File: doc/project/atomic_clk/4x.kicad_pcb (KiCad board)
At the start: 2 copper layers, 97.5 x 62.5 mm, 88 parts, among them J1 Goldpin, J2 Bat, SW1 POWER, SW2 SET, SW3 CLEAR, U1 BQ-M322RD, U2 STM32F030F4Px, U3 TC1185-3.3VCT8, Y1 18.432MHz

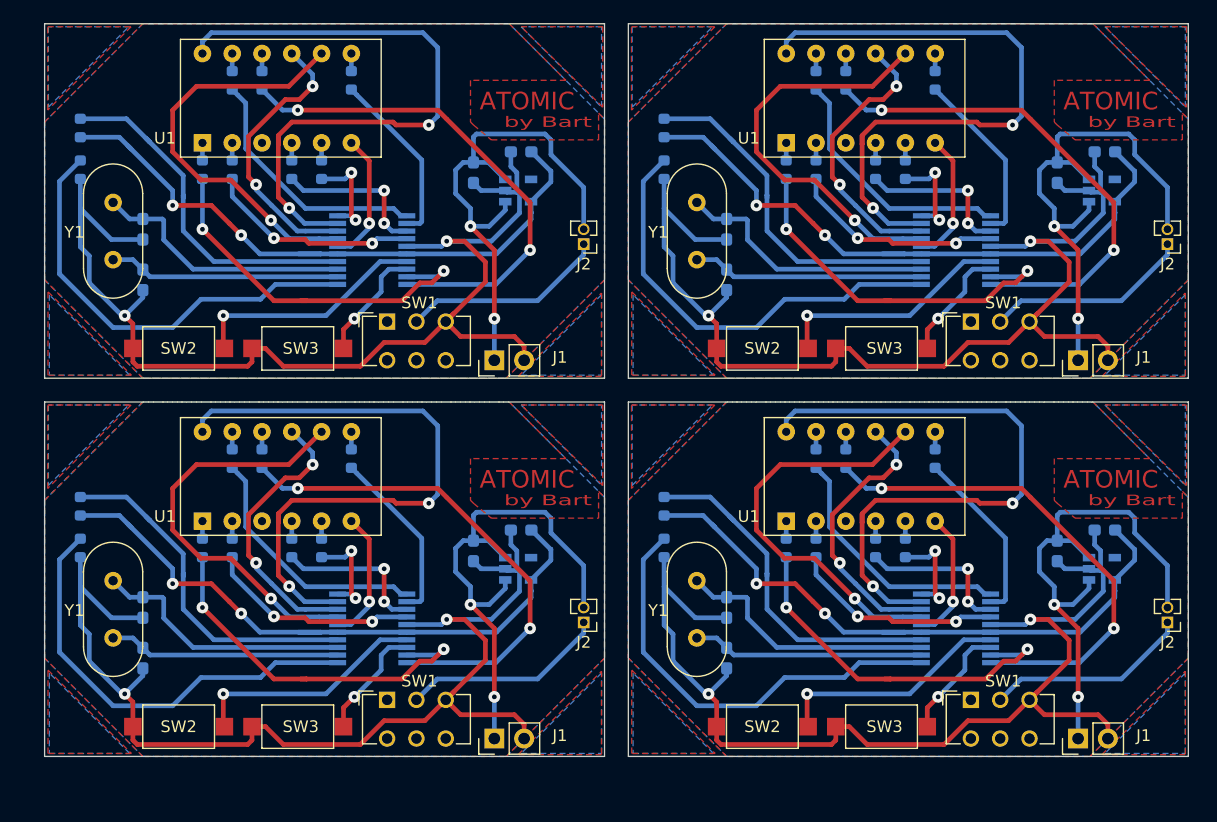
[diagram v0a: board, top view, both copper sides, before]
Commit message: correct pads for battery
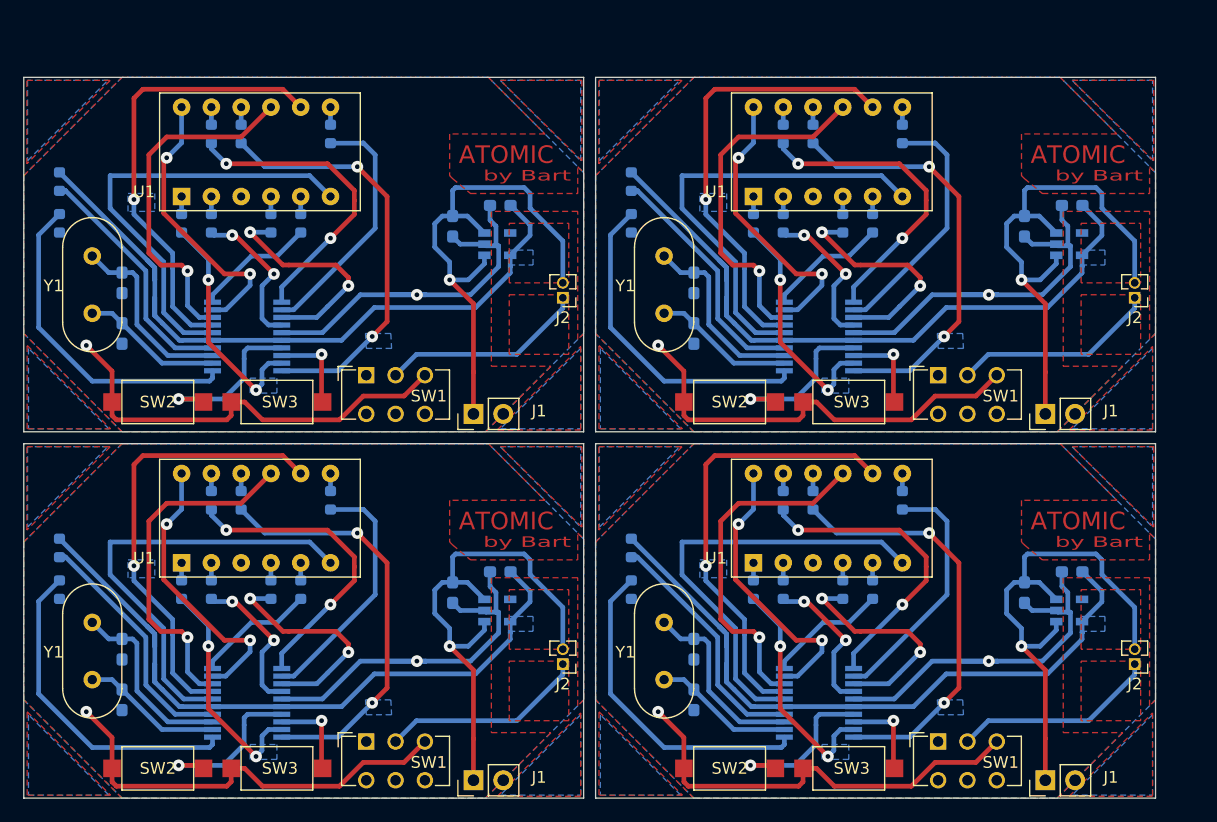
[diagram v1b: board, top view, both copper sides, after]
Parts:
- removed the C1 at (226.3, 131.3)
- removed the C1 at (226.3, 99.1)
- removed the C1 at (176.5, 99.1)
- removed the C1 at (176.5, 131.3)
- removed the C2 at (226.3, 127.0)
- removed the C2 at (226.3, 94.7)
- removed the C2 at (176.5, 94.7)
- removed the C2 at (176.5, 127.0)
- removed the C3 at (254.5, 122.2)
- removed the C3 at (254.5, 89.9)
- removed the C3 at (204.7, 89.9)
- removed the C3 at (204.7, 122.2)
- removed the C4 at (258.6, 120.4)
- removed the C4 at (258.6, 88.1)
- removed the C4 at (208.8, 88.1)
- removed the C4 at (208.8, 120.4)
- removed the J1 at (256.3, 138.2)
- removed the J1 at (256.3, 105.9)
- removed the J1 at (206.5, 105.9)
- removed the J1 at (206.5, 138.2)
- removed the J2 at (263.9, 128.3)
- removed the J2 at (263.9, 96.0)
- removed the J2 at (214.1, 96.0)
- removed the J2 at (214.1, 128.3)
- removed the R1 at (233.9, 114.3)
- removed the R1 at (233.9, 82.0)
- removed the R1 at (184.2, 82.0)
- removed the R1 at (184.2, 114.3)
- removed the R2 at (244.1, 114.3)
- removed the R2 at (244.1, 82.0)
- removed the R2 at (194.3, 82.0)
- removed the R2 at (194.3, 114.3)
- removed the R3 at (239.0, 121.9)
- removed the R3 at (239.0, 89.7)
- removed the R3 at (189.2, 89.7)
- removed the R3 at (189.2, 121.9)
- removed the R4 at (233.9, 121.9)
- removed the R4 at (233.9, 89.7)
- removed the R4 at (184.2, 89.7)
- removed the R4 at (184.2, 121.9)
- removed the R5 at (231.4, 121.9)
- removed the R5 at (231.4, 89.7)
- removed the R5 at (181.6, 89.7)
- removed the R5 at (181.6, 121.9)
- removed the R6 at (236.5, 114.3)
- removed the R6 at (236.5, 82.0)
- removed the R6 at (186.7, 82.0)
- removed the R6 at (186.7, 114.3)
- removed the R7 at (241.6, 121.9)
- removed the R7 at (241.6, 89.7)
- removed the R7 at (191.8, 89.7)
- removed the R7 at (191.8, 121.9)
- removed the R8 at (221.0, 121.9)
- removed the R8 at (221.0, 89.7)
- removed the R8 at (171.2, 89.7)
- removed the R8 at (171.2, 121.9)
- removed the R9 at (221.0, 118.4)
- removed the R9 at (221.0, 86.1)
- removed the R9 at (171.2, 86.1)
- removed the R9 at (171.2, 118.4)
- removed the SW1 at (247.1, 134.9)
- removed the SW1 at (247.1, 102.6)
- removed the SW1 at (197.4, 102.6)
- removed the SW1 at (197.4, 134.9)
- removed the SW2 at (229.4, 137.2)
- removed the SW2 at (229.4, 104.9)
- removed the SW2 at (179.6, 104.9)
- removed the SW2 at (179.6, 137.2)
- removed the SW3 at (239.5, 137.2)
- removed the SW3 at (239.5, 104.9)
- removed the SW3 at (189.7, 104.9)
- removed the SW3 at (189.7, 137.2)
- removed the U1 at (231.4, 119.6)
- removed the U1 at (231.4, 87.4)
- removed the U1 at (181.6, 87.4)
- removed the U1 at (181.6, 119.6)
- removed the U2 at (245.9, 128.8)
- removed the U2 at (245.9, 96.5)
- removed the U2 at (196.1, 96.5)
- removed the U2 at (196.1, 128.8)
- removed the U3 at (258.3, 123.7)
- removed the U3 at (258.3, 91.4)
- removed the U3 at (208.5, 91.4)
- removed the U3 at (208.5, 123.7)
- removed the Y1 at (223.8, 124.7)
- removed the Y1 at (223.8, 92.5)
- removed the Y1 at (174.0, 92.5)
- removed the Y1 at (174.0, 124.7)
- added C1: 22p, Capacitor_SMD:C_0603_1608Metric_Pad1.05x0.95mm_HandSolder, B.Cu at (174.8, 134.9)
- added C1: 22p, Capacitor_SMD:C_0603_1608Metric_Pad1.05x0.95mm_HandSolder, B.Cu at (174.8, 103.6)
- added C1: 22p, Capacitor_SMD:C_0603_1608Metric_Pad1.05x0.95mm_HandSolder, B.Cu at (223.5, 103.6)
- added C1: 22p, Capacitor_SMD:C_0603_1608Metric_Pad1.05x0.95mm_HandSolder, B.Cu at (223.5, 134.9)
- added C2: 22p, Capacitor_SMD:C_0603_1608Metric_Pad1.05x0.95mm_HandSolder, B.Cu at (174.8, 130.6)
- added C2: 22p, Capacitor_SMD:C_0603_1608Metric_Pad1.05x0.95mm_HandSolder, B.Cu at (174.8, 99.3)
- added C2: 22p, Capacitor_SMD:C_0603_1608Metric_Pad1.05x0.95mm_HandSolder, B.Cu at (223.5, 99.3)
- added C2: 22p, Capacitor_SMD:C_0603_1608Metric_Pad1.05x0.95mm_HandSolder, B.Cu at (223.5, 130.6)
- added C3: 100n, Capacitor_SMD:C_0603_1608Metric_Pad1.05x0.95mm_HandSolder, B.Cu at (202.9, 125.7)
- added C3: 100n, Capacitor_SMD:C_0603_1608Metric_Pad1.05x0.95mm_HandSolder, B.Cu at (202.9, 94.5)
- added C3: 100n, Capacitor_SMD:C_0603_1608Metric_Pad1.05x0.95mm_HandSolder, B.Cu at (251.7, 94.5)
- added C3: 100n, Capacitor_SMD:C_0603_1608Metric_Pad1.05x0.95mm_HandSolder, B.Cu at (251.7, 125.7)
- added C4: 100n, Capacitor_SMD:C_0603_1608Metric_Pad1.05x0.95mm_HandSolder, B.Cu at (207.0, 124.0)
- added C4: 100n, Capacitor_SMD:C_0603_1608Metric_Pad1.05x0.95mm_HandSolder, B.Cu at (207.0, 92.7)
- added C4: 100n, Capacitor_SMD:C_0603_1608Metric_Pad1.05x0.95mm_HandSolder, B.Cu at (255.8, 92.7)
- added C4: 100n, Capacitor_SMD:C_0603_1608Metric_Pad1.05x0.95mm_HandSolder, B.Cu at (255.8, 124.0)
- added J1: Goldpin, Connector_PinHeader_2.54mm:PinHeader_1x02_P2.54mm_Vertical, F.Cu at (204.7, 141.7)
- added J1: Goldpin, Connector_PinHeader_2.54mm:PinHeader_1x02_P2.54mm_Vertical, F.Cu at (204.7, 110.5)
- added J1: Goldpin, Connector_PinHeader_2.54mm:PinHeader_1x02_P2.54mm_Vertical, F.Cu at (253.5, 110.5)
- added J1: Goldpin, Connector_PinHeader_2.54mm:PinHeader_1x02_P2.54mm_Vertical, F.Cu at (253.5, 141.7)
- added J2: Bat, Connector_PinHeader_1.27mm:PinHeader_1x02_P1.27mm_Vertical, F.Cu at (212.3, 131.8)
- added J2: Bat, Connector_PinHeader_1.27mm:PinHeader_1x02_P1.27mm_Vertical, F.Cu at (212.3, 100.6)
- added J2: Bat, Connector_PinHeader_1.27mm:PinHeader_1x02_P1.27mm_Vertical, F.Cu at (261.1, 100.6)
- added J2: Bat, Connector_PinHeader_1.27mm:PinHeader_1x02_P1.27mm_Vertical, F.Cu at (261.1, 131.8)
- added R1: 120, Resistor_SMD:R_0603_1608Metric, B.Cu at (182.4, 117.9)
- added R1: 120, Resistor_SMD:R_0603_1608Metric, B.Cu at (182.4, 86.6)
- added R1: 120, Resistor_SMD:R_0603_1608Metric, B.Cu at (231.1, 86.6)
- added R1: 120, Resistor_SMD:R_0603_1608Metric, B.Cu at (231.1, 117.9)
- added R2: 120, Resistor_SMD:R_0603_1608Metric, B.Cu at (192.5, 117.9)
- added R2: 120, Resistor_SMD:R_0603_1608Metric, B.Cu at (192.5, 86.6)
- added R2: 120, Resistor_SMD:R_0603_1608Metric, B.Cu at (241.3, 86.6)
- added R2: 120, Resistor_SMD:R_0603_1608Metric, B.Cu at (241.3, 117.9)
- added R3: 120, Resistor_SMD:R_0603_1608Metric, B.Cu at (187.5, 125.5)
- added R3: 120, Resistor_SMD:R_0603_1608Metric, B.Cu at (187.5, 94.2)
- added R3: 120, Resistor_SMD:R_0603_1608Metric, B.Cu at (236.2, 94.2)
- added R3: 120, Resistor_SMD:R_0603_1608Metric, B.Cu at (236.2, 125.5)
- added R4: 120, Resistor_SMD:R_0603_1608Metric, B.Cu at (182.4, 125.5)
- added R4: 120, Resistor_SMD:R_0603_1608Metric, B.Cu at (182.4, 94.2)
- added R4: 120, Resistor_SMD:R_0603_1608Metric, B.Cu at (231.1, 94.2)
- added R4: 120, Resistor_SMD:R_0603_1608Metric, B.Cu at (231.1, 125.5)
- added R5: 120, Resistor_SMD:R_0603_1608Metric, B.Cu at (179.8, 125.5)
- added R5: 120, Resistor_SMD:R_0603_1608Metric, B.Cu at (179.8, 94.2)
- added R5: 120, Resistor_SMD:R_0603_1608Metric, B.Cu at (228.6, 94.2)
- added R5: 120, Resistor_SMD:R_0603_1608Metric, B.Cu at (228.6, 125.5)
- added R6: 120, Resistor_SMD:R_0603_1608Metric, B.Cu at (184.9, 117.9)
- added R6: 120, Resistor_SMD:R_0603_1608Metric, B.Cu at (184.9, 86.6)
- added R6: 120, Resistor_SMD:R_0603_1608Metric, B.Cu at (233.7, 86.6)
- added R6: 120, Resistor_SMD:R_0603_1608Metric, B.Cu at (233.7, 117.9)
- added R7: 120, Resistor_SMD:R_0603_1608Metric, B.Cu at (190.0, 125.5)
- added R7: 120, Resistor_SMD:R_0603_1608Metric, B.Cu at (190.0, 94.2)
- added R7: 120, Resistor_SMD:R_0603_1608Metric, B.Cu at (238.8, 94.2)
- added R7: 120, Resistor_SMD:R_0603_1608Metric, B.Cu at (238.8, 125.5)
- added R8: 10k, Resistor_SMD:R_0603_1608Metric, B.Cu at (169.4, 125.5)
- added R8: 10k, Resistor_SMD:R_0603_1608Metric, B.Cu at (169.4, 94.2)
- added R8: 10k, Resistor_SMD:R_0603_1608Metric, B.Cu at (218.2, 94.2)
- added R8: 10k, Resistor_SMD:R_0603_1608Metric, B.Cu at (218.2, 125.5)
- added R9: 10k, Resistor_SMD:R_0603_1608Metric, B.Cu at (169.4, 121.9)
- added R9: 10k, Resistor_SMD:R_0603_1608Metric, B.Cu at (169.4, 90.7)
- added R9: 10k, Resistor_SMD:R_0603_1608Metric, B.Cu at (218.2, 90.7)
- added R9: 10k, Resistor_SMD:R_0603_1608Metric, B.Cu at (218.2, 121.9)
- added SW1: POWER, Button_Switch_THT:SW_CuK_JS202011CQN_DPDT_Straight, F.Cu at (195.6, 138.4)
- added SW1: POWER, Button_Switch_THT:SW_CuK_JS202011CQN_DPDT_Straight, F.Cu at (195.6, 107.2)
- added SW1: POWER, Button_Switch_THT:SW_CuK_JS202011CQN_DPDT_Straight, F.Cu at (244.3, 107.2)
- added SW1: POWER, Button_Switch_THT:SW_CuK_JS202011CQN_DPDT_Straight, F.Cu at (244.3, 138.4)
- added SW2: SET, Button_Switch_SMD:SW_SPST_CK_RS282G05A3, F.Cu at (177.8, 140.7)
- added SW2: SET, Button_Switch_SMD:SW_SPST_CK_RS282G05A3, F.Cu at (177.8, 109.5)
- added SW2: SET, Button_Switch_SMD:SW_SPST_CK_RS282G05A3, F.Cu at (226.6, 109.5)
- added SW2: SET, Button_Switch_SMD:SW_SPST_CK_RS282G05A3, F.Cu at (226.6, 140.7)
- added SW3: CLEAR, Button_Switch_SMD:SW_SPST_CK_RS282G05A3, F.Cu at (188.0, 140.7)
- added SW3: CLEAR, Button_Switch_SMD:SW_SPST_CK_RS282G05A3, F.Cu at (188.0, 109.5)
- added SW3: CLEAR, Button_Switch_SMD:SW_SPST_CK_RS282G05A3, F.Cu at (236.7, 109.5)
- added SW3: CLEAR, Button_Switch_SMD:SW_SPST_CK_RS282G05A3, F.Cu at (236.7, 140.7)
- added U1: BQ-M322RD, Display_7Segment:MAN3420A, F.Cu at (179.8, 123.2)
- added U1: BQ-M322RD, Display_7Segment:MAN3420A, F.Cu at (179.8, 91.9)
- added U1: BQ-M322RD, Display_7Segment:MAN3420A, F.Cu at (228.6, 91.9)
- added U1: BQ-M322RD, Display_7Segment:MAN3420A, F.Cu at (228.6, 123.2)
- added U2: STM32F030F4Px, Package_SO:TSSOP-20_4.4x6.5mm_P0.65mm, B.Cu at (185.4, 135.1)
- added U2: STM32F030F4Px, Package_SO:TSSOP-20_4.4x6.5mm_P0.65mm, B.Cu at (185.4, 103.9)
- added U2: STM32F030F4Px, Package_SO:TSSOP-20_4.4x6.5mm_P0.65mm, B.Cu at (234.2, 103.9)
- added U2: STM32F030F4Px, Package_SO:TSSOP-20_4.4x6.5mm_P0.65mm, B.Cu at (234.2, 135.1)
- added U3: TC1185-3.3VCT8, Package_TO_SOT_SMD:SOT-23-5, B.Cu at (206.8, 127.3)
- added U3: TC1185-3.3VCT8, Package_TO_SOT_SMD:SOT-23-5, B.Cu at (206.8, 96.0)
- added U3: TC1185-3.3VCT8, Package_TO_SOT_SMD:SOT-23-5, B.Cu at (255.5, 96.0)
- added U3: TC1185-3.3VCT8, Package_TO_SOT_SMD:SOT-23-5, B.Cu at (255.5, 127.3)
- added Y1: 18.432MHz, Crystal:Crystal_HC49-4H_Vertical, F.Cu at (172.2, 128.3)
- added Y1: 18.432MHz, Crystal:Crystal_HC49-4H_Vertical, F.Cu at (172.2, 97.0)
- added Y1: 18.432MHz, Crystal:Crystal_HC49-4H_Vertical, F.Cu at (221.0, 97.0)
- added Y1: 18.432MHz, Crystal:Crystal_HC49-4H_Vertical, F.Cu at (221.0, 128.3)
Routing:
- net (no net): track 0.00 -> 1739.5 mm, vias 0 -> 57
- net GND: track 391.7 -> 71.0 mm, vias 8 -> 2
- net D1: track 216.7 -> 24.2 mm, vias 8 -> 2
- net +3V3: track 217.2 -> 59.6 mm, vias 8 -> 0
- net SF: track 170.5 -> 35.7 mm, vias 8 -> 2
- net Net-(C3-Pad1): track 179.3 -> 44.8 mm, vias 8 -> 1
- net Net-(R8-Pad1): track 150.4 -> 27.9 mm
- net SE: track 130.5 -> 20.3 mm, vias 8 -> 2
- net D3: track 141.6 -> 38.4 mm, vias 4 -> 1
- net Net-(R9-Pad2): track 121.9 -> 21.3 mm
- net Net-(C2-Pad1): track 89.9 -> 16.2 mm
- net Net-(SW2-Pad1): track 81.6 -> 14.4 mm, vias 4 -> 1
- net Net-(C1-Pad1): track 79.0 -> 12.0 mm
- net D2: track 94.2 -> 29.9 mm, vias 8 -> 1
- net SA: track 86.5 -> 26.5 mm, vias 0 -> 2
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- added copper zone on B.Cu, net +3V3
- added copper zone on B.Cu, net D3
- added copper zone on F.Cu, net Net-(C3-Pad1)
- added copper zone on F.Cu, net Net-(J2-Pad1)
- added copper zone on B.Cu, net SE
- added copper zone on B.Cu, net SF
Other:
- board size 97.5 x 62.5 mm -> 96.5 x 61.5 mm
